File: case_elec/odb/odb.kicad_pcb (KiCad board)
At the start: 2 copper layers, 98 x 79 mm, 10 parts, among them J1 Screw_Terminal_01x02, J2 Conn_02x07_Top_Bottom, SW1 SW_SPST, SW2 SW_SPST, U1 REYAX RYLR896, U2 BNO055, U3 MPL3115A, U4 Ultimate_GPS, U5 Teensy3.5

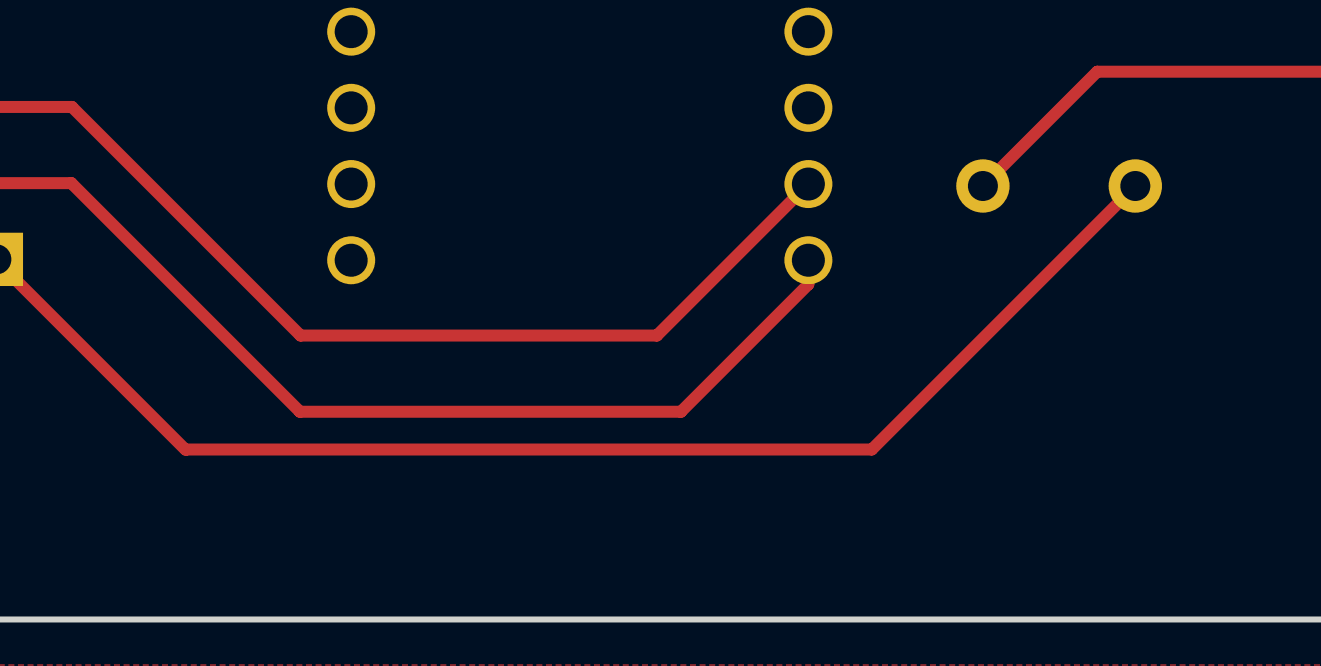
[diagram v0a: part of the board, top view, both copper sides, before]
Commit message: Correction d'espacement + nettoyage du file system du projet
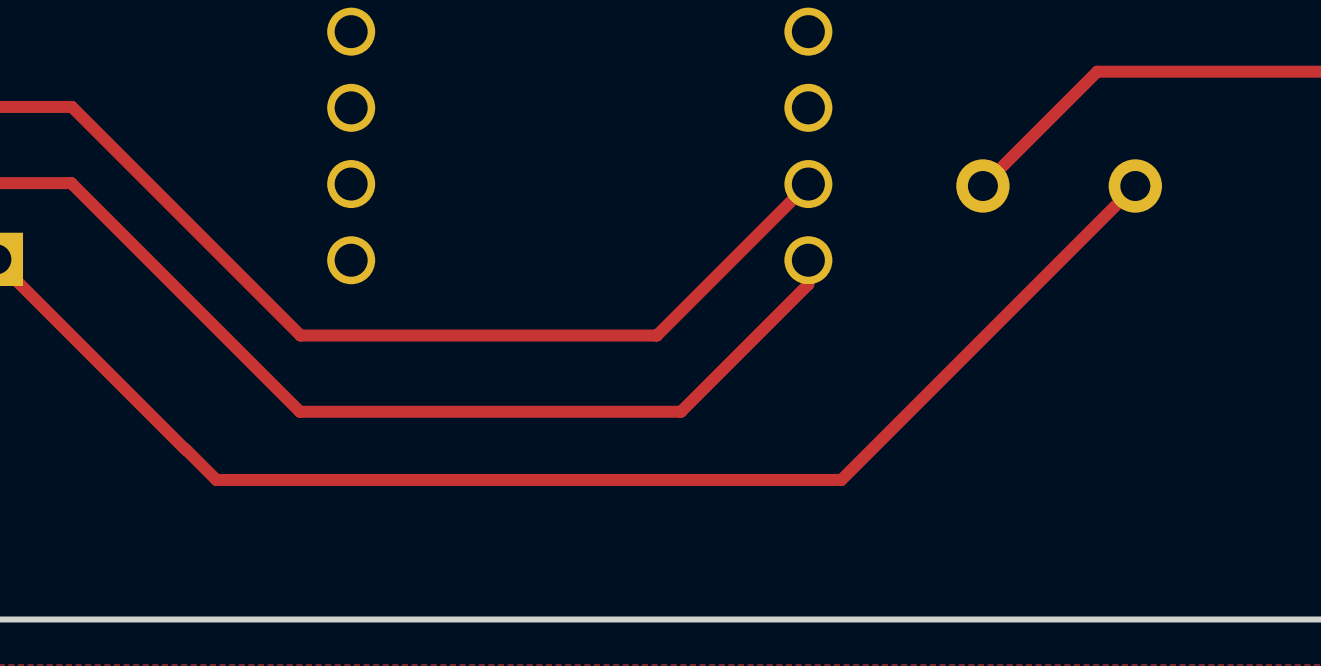
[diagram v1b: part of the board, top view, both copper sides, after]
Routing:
- net Net-(SW2-Pad1): track 44.2 -> 45.1 mm
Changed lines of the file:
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@@
     (pts (xy 198.247 56.769) (xy 198.247 135.769))
     (height -7.493)
-    (gr_text "79.0000 mm" (at 204.59 96.269 90) (layer "User.1")
+    (gr_text "79,0000 mm" (at 204.59 96.269 90) (layer "User.1")
       (effects (font (size 1 1) (thickness 0.15)))
     )
@@
     (pts (xy 100.203 56.769) (xy 198.247 56.769))
     (height -5.969)
-    (gr_text "98.0440 mm" (at 149.225 49.65) (layer "User.1")
+    (gr_text "98,0440 mm" (at 149.225 49.65) (layer "User.1")
       (effects (font (size 1 1) (thickness 0.15)))
     )
@@
     (pts (xy 198.374 135.89) (xy 198.374 131.318))
     (height 12.954)
-    (gr_text "4.5720 mm" (at 210.178 133.604 90) (layer "User.1")
+    (gr_text "4,5720 mm" (at 210.178 133.604 90) (layer "User.1")
       (effects (font (size 1 1) (thickness 0.15)))
     )
@@
   (segment (start 174.535094 114.456406) (end 167.672 121.3195) (width 0.4) (layer "F.Cu") (net 17))
   (segment (start 163.862 117.5095) (end 167.672 121.3195) (width 0.4) (layer "F.Cu") (net 17))
-  (segment (start 123.328107 130.103393) (end 146.188107 130.103393) (width 0.4) (layer "F.Cu") (net 18))
   (segment (start 117.007 123.7645) (end 117.007 123.8045) (width 0.4) (layer "F.Cu") (net 18))
-  (segment (start 146.188107 130.103393) (end 154.972 121.3195) (width 0.4) (layer "F.Cu") (net 18))
+  (segment (start 124.342694 131.11798) (end 145.17352 131.11798) (width 0.4) (layer "F.Cu") (net 18))
+  (segment (start 123.328107 130.103393) (end 124.342694 131.11798) (width 0.4) (layer "F.Cu") (net 18))
   (segment (start 117.007 123.8045) (end 123.317 130.1145) (width 0.4) (layer "F.Cu") (net 18))
-  (segment (start 127.127 128.8445) (end 139.827 128.8445) (width 0.4) (layer "F.Cu") (net 20))
+  (segment (start 145.17352 131.11798) (end 154.972 121.3195) (width 0.4) (layer "F.Cu") (net 18))
   (segment (start 114.427 121.2245) (end 119.507 121.2245) (width 0.4) (layer "F.Cu") (net 20))
   (segment (start 119.507 121.2245) (end 127.127 128.8445) (width 0.4) (layer "F.Cu") (net 20))
+  (segment (start 111.887 123.7645) (end 114.427 121.2245) (width 0.4) (layer "F.Cu") (net 20))
   (segment (start 144.074067 124.597433) (end 144.074067 123.794442) (width 0.4) (layer "F.Cu") (net 20))
   (segment (start 139.827 128.8445) (end 144.074067 124.597433) (width 0.4) (layer "F.Cu") (net 20))
-  (segment (start 111.887 123.7645) (end 114.427 121.2245) (width 0.4) (layer "F.Cu") (net 20))
+  (segment (start 127.127 128.8445) (end 139.827 128.8445) (width 0.4) (layer "F.Cu") (net 20))
   (segment (start 119.526256 118.6845) (end 127.146256 126.3045) (width 0.4) (layer "F.Cu") (net 21))
   (segment (start 127.146256 126.3045) (end 139.024009 126.3045) (width 0.4) (layer "F.Cu") (net 21))
@@
       00788908-d6f1-4bb1-91d2-298090d0c3e6
       069b20a4-a897-47eb-a3dc-f8ba8d815d24
-      08125349-5a9b-45b9-8b80-e85ab05860bd
       098c33ae-2ab5-449e-a7c4-a00f109ace54
       0c50eab7-39ae-4c58-a2d7-88b23b2fe0f1
-      0c534034-7511-49ed-ae3c-398b60200511
       0eb1056a-8f63-4949-9ef8-3344cf502619
       1641ecf6-8efd-4ffd-9e36-6b63a6ac1142
@@
       56e7995d-d1db-47f7-a3fa-62cb78d54a88
       5ebdc48a-93d1-4939-a693-963e22bcf937
-      5fec2a6b-a6e0-4620-8aef-6f46ce2e3e45
       60a37cd1-1bb2-4be8-81fb-4ddffb697632
       663a0fb4-4b5e-418a-8050-04386ad872a4
       68aa0d32-d4df-4a80-afe2-622555e58199
-      68ba5c4f-768f-41f4-b905-4c8a917903ca
       68e4f182-94d6-4ed9-887e-3aa8b7fa4365
       6920a7a4-b26f-4bf9-957a-c806fd46a74e
@@
       7cb02bdb-f394-44e5-89c5-10bdba437945
       7cf01ef7-a66f-4276-9533-ec405a7d5ec0
-      7da3685c-03a0-4aae-b35c-c7e594ff9dee
       7df9d31e-8deb-411c-935d-bd97b797cd97
-      7e8f58ae-58bd-471f-ab44-0dd445d2ba75
       84472fb8-c821-49c1-b51a-bd1937926415
       8995ae63-a5c6-47c4-8b8f-9c1278c3d26a
       8ae04767-364d-416b-8810-8e5e3049ad62
       8b3e42fa-9345-4cae-9afb-9ec4acf89dd3
-      8b9c7e3e-7c42-4167-abfc-d0223bb81cbc
       8dfa0cb5-1602-4f40-ba50-9c6daba8533e
       92dc9416-a309-48f4-94b2-202d16c50d54
@@
       d27421b6-f6f6-4084-8e5e-af589c6b4afd
       da8db3f9-e3c7-4ddd-8329-5f3e44e1fb28
-      dae48166-d7d0-4e7b-a342-dc7a89aaeae4
       e07de352-5865-4ce6-9a72-11b46da94316
       e3183def-855c-4601-99d6-e3f99d664a99

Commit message: amélioration route sw
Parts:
- moved SW2 20.1 mm to (147.4, 129.4), turned to 0 degrees
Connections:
- SW2 pad 2: +5V -> Net-(J1-Pad1)
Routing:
- net +5V: track 193.0 -> 177.4 mm
- net Net-(J1-Pad1): track 24.9 -> 37.8 mm
- net Net-(SW2-Pad1): track 45.1 -> 44.3 mm
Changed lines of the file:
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@@
   )
   (footprint "common_misc:SW" (layer "B.Cu")
-    (at 162.592 116.2395 180)
+    (at 147.415 129.445)
     (property "Sheetfile" "odb.kicad_sch")
     (property "Sheetname" "")
     (attr smd)
-    (fp_text reference "SW2" (at -12.7 7.62 unlocked) (layer "B.SilkS")
+    (fp_text reference "SW2" (at 4.985 -4.985 -180 unlocked) (layer "B.SilkS")
       (effects (font (size 1 1) (thickness 0.15)) (justify mirror))
     )
-    (fp_text value "SW_SPST" (at -12.7 6.12 unlocked) (layer "B.Fab")
+    (fp_text value "SW_SPST" (at 4.985 -6.485 -180 unlocked) (layer "B.Fab")
       (effects (font (size 1 1) (thickness 0.15)) (justify mirror))
     )
-    (fp_text user "${REFERENCE}" (at -12.7 4.62 unlocked) (layer "B.Fab")
+    (fp_text user "${REFERENCE}" (at 4.985 -7.985 -180 unlocked) (layer "B.Fab")
       (effects (font (size 1 1) (thickness 0.15)) (justify mirror))
     )
@@
     (fp_line (start 15.24 -10.16) (end 0 -10.16) (layer "B.SilkS") (width 0.12))
     (fp_line (start 15.24 0) (end 15.24 -10.16) (layer "B.SilkS") (width 0.12))
-    (pad "1" thru_hole circle (at 7.62 -5.08 90) (size 1.778 1.778) (drill 1) (layers *.Cu *.Mask)
+    (pad "1" thru_hole circle (at 7.62 -5.08 270) (size 1.778 1.778) (drill 1) (layers *.Cu *.Mask)
       (net 18 "Net-(SW2-Pad1)") (pinfunction "A") (pintype "passive") (solder_mask_margin 0.0508))
-    (pad "2" thru_hole circle (at 12.7 -5.08 90) (size 1.778 1.778) (drill 1) (layers *.Cu *.Mask)
-      (net 17 "+5V") (pinfunction "B") (pintype "passive") (solder_mask_margin 0.0508))
+    (pad "2" thru_hole circle (at 12.7 -5.08 270) (size 1.778 1.778) (drill 1) (layers *.Cu *.Mask)
+      (net 1 "Net-(J1-Pad1)") (pinfunction "B") (pintype "passive") (solder_mask_margin 0.0508))
   )
   (footprint "TerminalBlock_Phoenix:TerminalBlock_Phoenix_MKDS-1,5-2-5.08_1x02_P5.08mm_Horizontal" (layer "B.Cu")
@@
     (style (thickness 0.15) (arrow_length 1.27) (text_position_mode 0) (extension_height 0.58642) (extension_offset 0.5) keep_text_aligned)
   )
+  (segment (start 172.0565 124.365) (end 160.115 124.365) (width 0.4) (layer "F.Cu") (net 1))
   (segment (start 175.387 126.3045) (end 188.087 126.3045) (width 0.4) (layer "F.Cu") (net 1))
+  (segment (start 172.752 123.6695) (end 172.0565 124.365) (width 0.4) (layer "F.Cu") (net 1))
   (segment (start 190.627 123.7645) (end 190.627 121.2245) (width 0.4) (layer "F.Cu") (net 1))
   (segment (start 188.087 126.3045) (end 190.627 123.7645) (width 0.4) (layer "F.Cu") (net 1))
@@
   (segment (start 174.535094 106.836406) (end 174.535094 114.456406) (width 0.4) (layer "F.Cu") (net 17))
   (segment (start 180.467 100.9045) (end 174.535094 106.836406) (width 0.4) (layer "F.Cu") (net 17))
-  (segment (start 149.892 121.3195) (end 153.702 117.5095) (width 0.4) (layer "F.Cu") (net 17))
   (segment (start 152.4 67.864442) (end 157.373058 67.864442) (width 0.4) (layer "F.Cu") (net 17))
   (segment (start 167.386 62.4235) (end 195.707 90.7445) (width 0.4) (layer "F.Cu") (net 17))
@@
   (segment (start 157.373058 67.864442) (end 162.814 62.4235) (width 0.4) (layer "F.Cu") (net 17))
   (segment (start 131.785008 62.4235) (end 162.814 62.4235) (width 0.4) (layer "F.Cu") (net 17))
-  (segment (start 153.702 117.5095) (end 163.862 117.5095) (width 0.4) (layer "F.Cu") (net 17))
   (segment (start 174.535094 114.456406) (end 167.672 121.3195) (width 0.4) (layer "F.Cu") (net 17))
   (segment (start 163.862 117.5095) (end 167.672 121.3195) (width 0.4) (layer "F.Cu") (net 17))
   (segment (start 117.007 123.7645) (end 117.007 123.8045) (width 0.4) (layer "F.Cu") (net 18))
   (segment (start 124.342694 131.11798) (end 145.17352 131.11798) (width 0.4) (layer "F.Cu") (net 18))
+  (segment (start 148.28202 131.11798) (end 147.32 131.11798) (width 0.4) (layer "F.Cu") (net 18))
   (segment (start 123.328107 130.103393) (end 124.342694 131.11798) (width 0.4) (layer "F.Cu") (net 18))
+  (segment (start 155.035 124.365) (end 148.28202 131.11798) (width 0.4) (layer "F.Cu") (net 18))
+  (segment (start 147.32 131.11798) (end 144.78 131.11798) (width 0.4) (layer "F.Cu") (net 18))
   (segment (start 117.007 123.8045) (end 123.317 130.1145) (width 0.4) (layer "F.Cu") (net 18))
-  (segment (start 145.17352 131.11798) (end 154.972 121.3195) (width 0.4) (layer "F.Cu") (net 18))
   (segment (start 114.427 121.2245) (end 119.507 121.2245) (width 0.4) (layer "F.Cu") (net 20))
   (segment (start 119.507 121.2245) (end 127.127 128.8445) (width 0.4) (layer "F.Cu") (net 20))
@@
       4cd9517a-a1b6-4e04-b930-c5822400160c
       4d712c32-a1bc-4207-b316-26158fc4749b
-      514186ce-7cfa-4c35-a3ae-047177127b0d
       515b593e-142d-48c0-b8b1-f6cff49acb5d
       55d1b95f-7e4e-41d8-94cc-f5b125db6641
@@
       c0f8d318-df04-4133-b370-482b7f72c484
       c2d491a4-3221-4c36-9bda-7a41df556609
-      c610dc33-664a-4ef4-9fd0-5765eabd1a3a
       c879037d-d5bb-4ac0-968b-eefd3f942914
-      cb257888-5ec6-44c2-8cdb-17ca06b83960
       cc9670c7-9bb5-4be1-951a-b4a367f8d9bc
       cdfe9250-ddc0-4de3-be5a-33a9e787a6dd

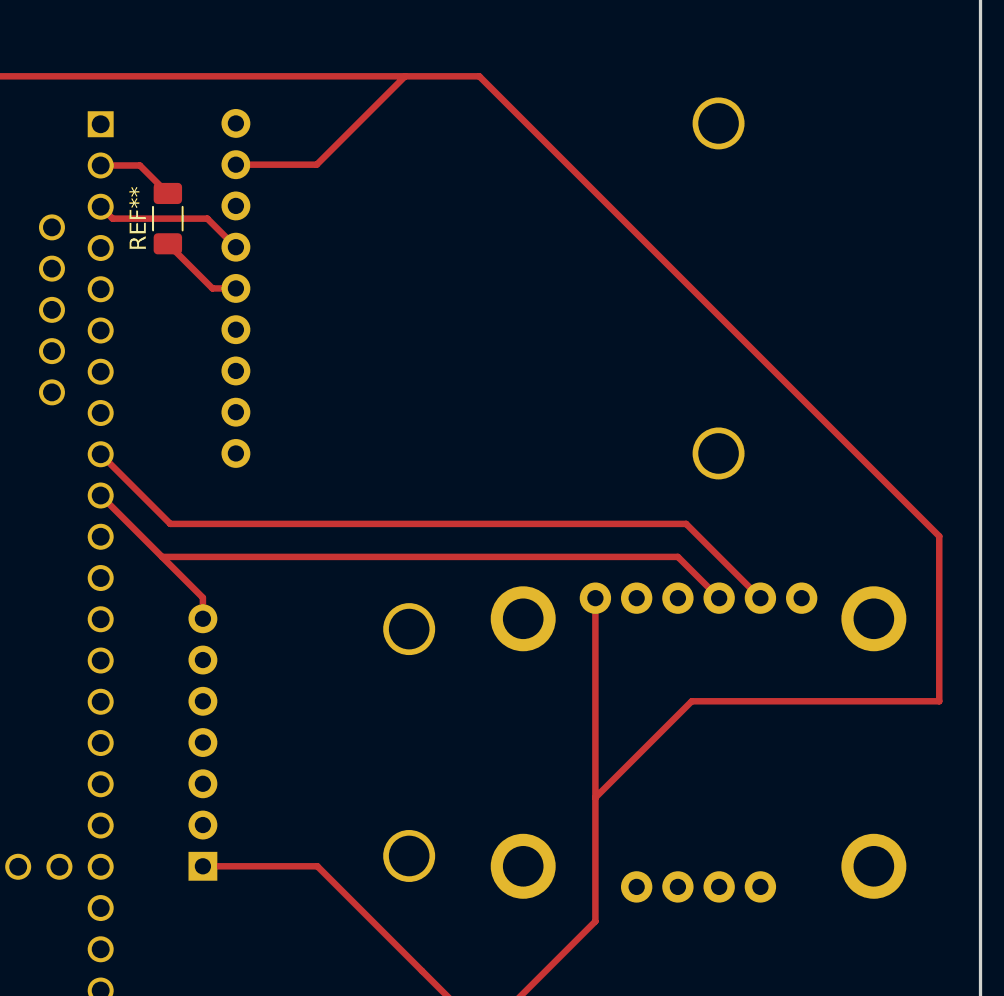
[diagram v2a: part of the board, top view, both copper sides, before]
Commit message: Nouveau mapping perçage + gerber
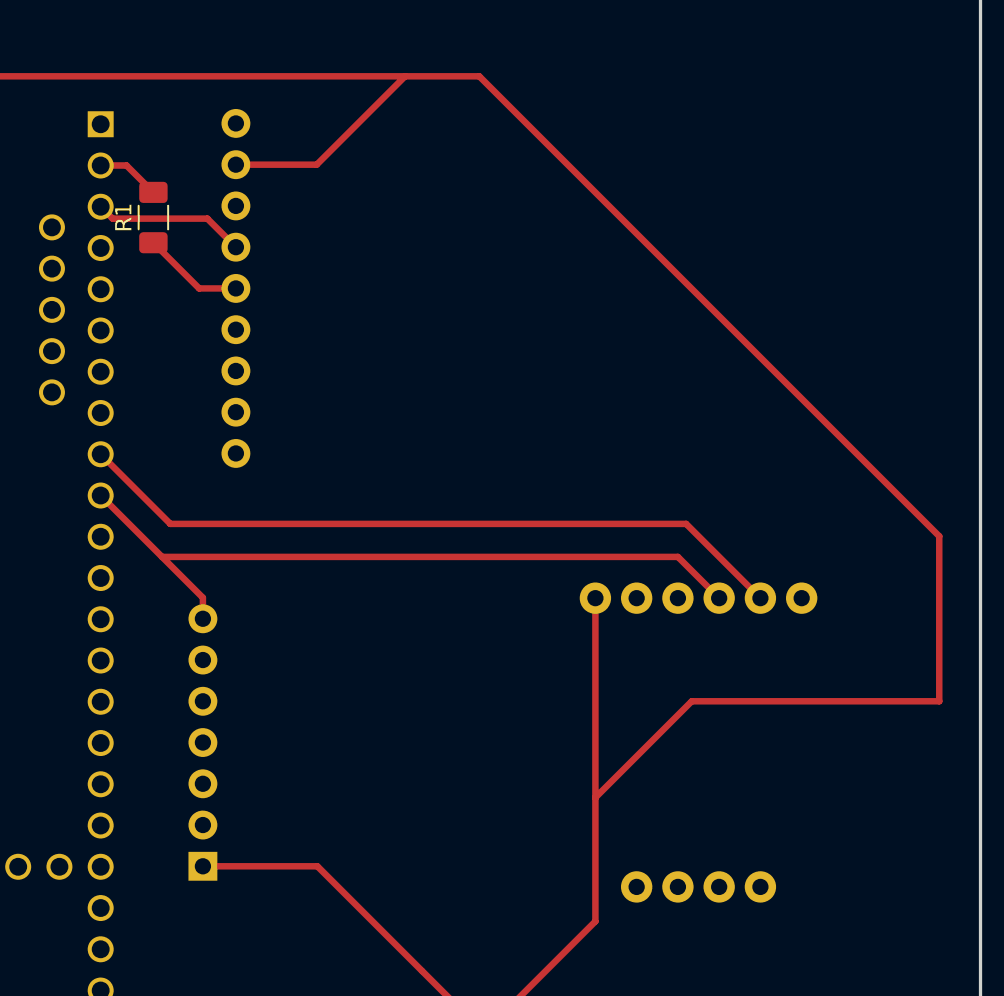
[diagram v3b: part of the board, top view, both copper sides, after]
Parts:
- removed REF**: R_1206, Resistor_SMD:R_1206_3216Metric_Pad1.30x1.75mm_HandSolder
- added R1: RESISTOR_1206, Resistor_SMD:R_1206_3216Metric_Pad1.30x1.75mm_HandSolder, F.Cu at (147.3, 71.1)
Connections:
- U4 pad 6: Net-(U4-Pad6) -> unconnected-(U4-Pad6)
- U5 pad 2: Net-(U4-Pad5) -> Net-(U5-Pad2)
- U5 pad 3: Net-(U4-Pad6) -> unconnected-(U4-Pad6)
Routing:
- net unconnected-(U4-Pad6): track 0.00 -> 9.36 mm
- net Net-(U4-Pad6): track 9.36 -> 0.00 mm
- net Net-(U4-Pad5): track 10.2 -> 6.25 mm
- net Net-(U5-Pad2): track 0.00 -> 3.93 mm
